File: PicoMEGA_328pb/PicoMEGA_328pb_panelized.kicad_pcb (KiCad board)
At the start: 2 copper layers, 100.2 x 94.2 mm, 416 parts, among them J1 ICSP, J2 3V3, J3 GPIO BLK A, J4 GPIO BLK B, J5 GPIO BLK C, J6 GPIO BLK D, U1 TPS62745DSSR, U2 ATmega328PB-MU, Y1 8Mhz

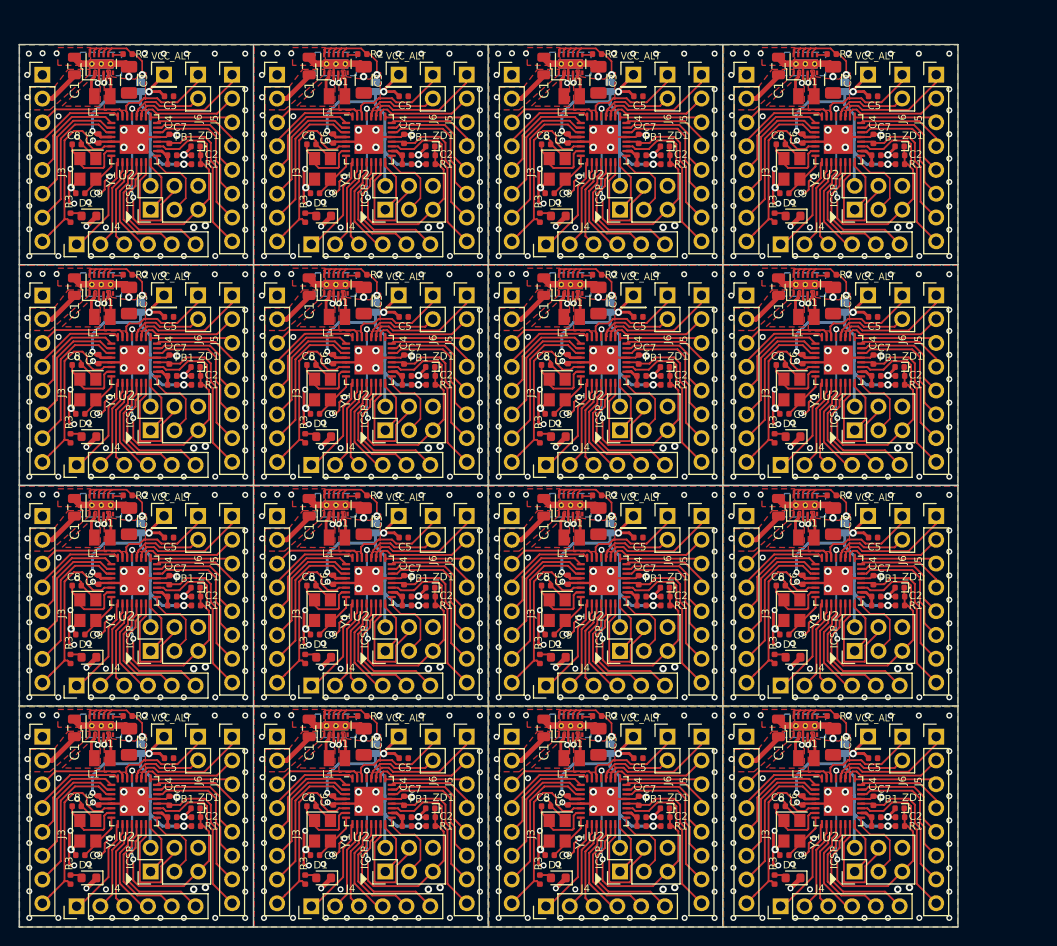
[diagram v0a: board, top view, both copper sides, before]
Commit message: PicoMEGA 328PB: rev0.1d
Fixed V_in regulator to use input voltage for enable to gurantee the
regulator powers on when an input voltage is applied.
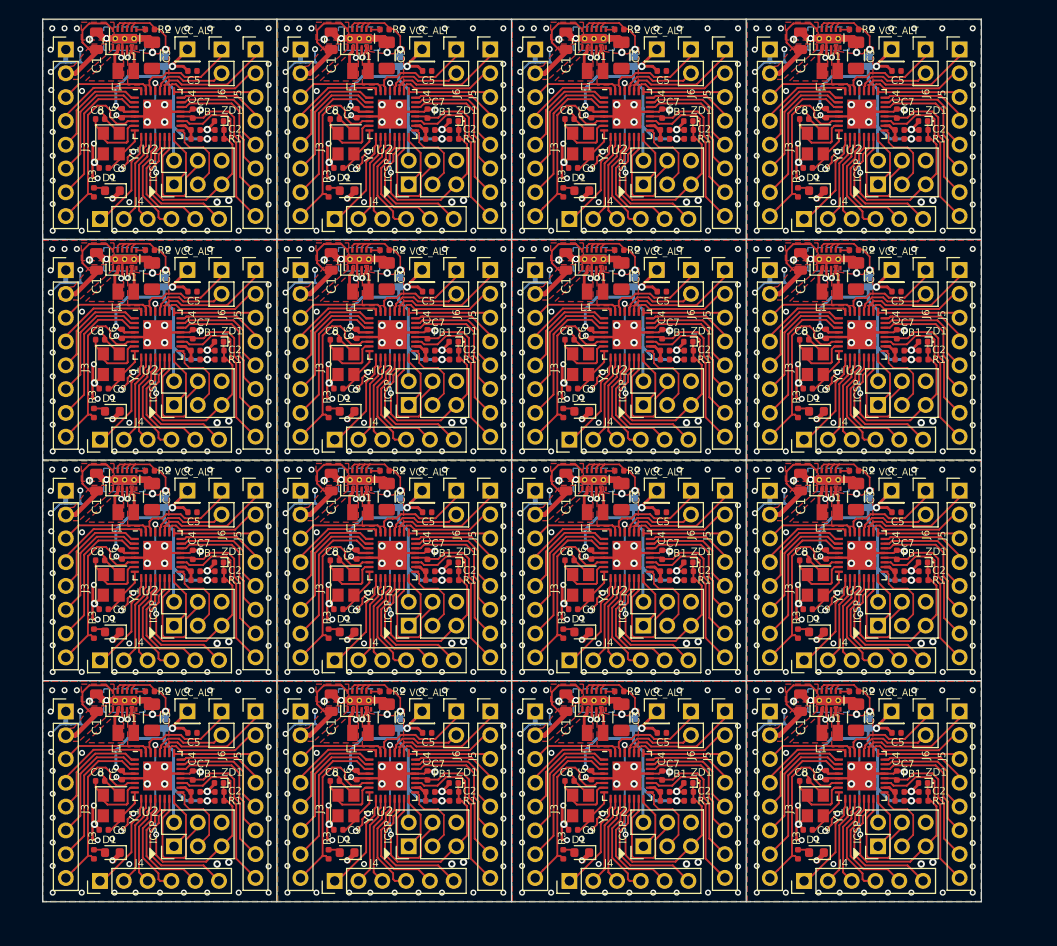
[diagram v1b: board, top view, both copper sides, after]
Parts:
- removed the C1 at (172.0, 124.6)
- removed the C1 at (121.9, 101.1)
- removed the C1 at (121.9, 77.5)
- removed the C1 at (121.9, 54.0)
- removed the C1 at (96.9, 124.6)
- removed the C1 at (96.9, 101.1)
- removed the C1 at (96.9, 77.5)
- removed the C1 at (172.0, 101.1)
- removed the C1 at (172.0, 77.5)
- removed the C1 at (172.0, 54.0)
- removed the C1 at (147.0, 124.6)
- removed the C1 at (147.0, 101.1)
- removed the C1 at (147.0, 77.5)
- removed the C1 at (147.0, 54.0)
- removed the C1 at (121.9, 124.6)
- removed the C2 at (185.0, 134.2)
- removed the C2 at (134.9, 110.6)
- removed the C2 at (134.9, 87.1)
- removed the C2 at (134.9, 63.5)
- removed the C2 at (109.8, 134.2)
- removed the C2 at (109.8, 110.6)
- removed the C2 at (109.8, 87.1)
- removed the C2 at (185.0, 110.6)
- removed the C2 at (185.0, 87.1)
- removed the C2 at (185.0, 63.5)
- removed the C2 at (160.0, 134.2)
- removed the C2 at (160.0, 110.6)
- removed the C2 at (160.0, 87.1)
- removed the C2 at (160.0, 63.5)
- removed the C2 at (134.9, 134.2)
- removed the C3 at (177.9, 126.1)
- removed the C3 at (127.8, 102.6)
- removed the C3 at (127.8, 79.0)
- removed the C3 at (127.8, 55.5)
- removed the C3 at (102.7, 126.1)
- removed the C3 at (102.7, 102.6)
- removed the C3 at (102.7, 79.0)
- removed the C3 at (177.9, 102.6)
- removed the C3 at (177.9, 79.0)
- removed the C3 at (177.9, 55.5)
- removed the C3 at (152.8, 126.1)
- removed the C3 at (152.8, 102.6)
- removed the C3 at (152.8, 79.0)
- removed the C3 at (152.8, 55.5)
- removed the C3 at (127.8, 126.1)
- removed the C4 at (182.2, 132.4)
- removed the C4 at (132.1, 108.9)
- removed the C4 at (132.1, 85.3)
- removed the C4 at (132.1, 61.8)
- removed the C4 at (107.0, 132.4)
- removed the C4 at (107.0, 108.9)
- removed the C4 at (107.0, 85.3)
- removed the C4 at (182.2, 108.9)
- removed the C4 at (182.2, 85.3)
- removed the C4 at (182.2, 61.8)
- removed the C4 at (157.1, 132.4)
- removed the C4 at (157.1, 108.9)
- removed the C4 at (157.1, 85.3)
- removed the C4 at (157.1, 61.8)
- removed the C4 at (132.1, 132.4)
- removed the C5 at (182.1, 127.9)
- removed the C5 at (132.0, 104.3)
- removed the C5 at (132.0, 80.8)
- removed the C5 at (132.0, 57.2)
- removed the C5 at (107.0, 127.9)
- removed the C5 at (107.0, 104.3)
- removed the C5 at (107.0, 80.8)
- removed the C5 at (182.1, 104.3)
- removed the C5 at (182.1, 80.8)
- removed the C5 at (182.1, 57.2)
- removed the C5 at (157.1, 127.9)
- removed the C5 at (157.1, 104.3)
- removed the C5 at (157.1, 80.8)
- removed the C5 at (157.1, 57.2)
- removed the C5 at (132.0, 127.9)
- removed the C6 at (174.6, 132.4)
- removed the C6 at (124.5, 108.8)
- removed the C6 at (124.5, 85.3)
- removed the C6 at (124.5, 61.7)
- removed the C6 at (99.5, 132.4)
- removed the C6 at (99.5, 108.8)
- removed the C6 at (99.5, 85.3)
- removed the C6 at (174.6, 108.8)
- removed the C6 at (174.6, 85.3)
- removed the C6 at (174.6, 61.7)
- removed the C6 at (149.6, 132.4)
- removed the C6 at (149.6, 108.8)
- removed the C6 at (149.6, 85.3)
- removed the C6 at (149.6, 61.7)
- removed the C6 at (124.5, 132.4)
- removed the C7 at (182.5, 134.2)
- removed the C7 at (132.4, 110.6)
- removed the C7 at (132.4, 87.1)
- removed the C7 at (132.4, 63.5)
- removed the C7 at (107.3, 134.2)
- removed the C7 at (107.3, 110.6)
- removed the C7 at (107.3, 87.1)
- removed the C7 at (182.5, 110.6)
- removed the C7 at (182.5, 87.1)
- removed the C7 at (182.5, 63.5)
- removed the C7 at (157.4, 134.2)
- removed the C7 at (157.4, 110.6)
- removed the C7 at (157.4, 87.1)
- removed the C7 at (157.4, 63.5)
- removed the C7 at (132.4, 134.2)
- removed the C8 at (172.3, 133.0)
- removed the C8 at (122.2, 109.4)
- removed the C8 at (122.2, 85.9)
- removed the C8 at (122.2, 62.3)
- removed the C8 at (97.1, 133.0)
- removed the C8 at (97.1, 109.4)
- removed the C8 at (97.1, 85.9)
- removed the C8 at (172.3, 109.4)
- removed the C8 at (172.3, 85.9)
- removed the C8 at (172.3, 62.3)
- removed the C8 at (147.2, 133.0)
- removed the C8 at (147.2, 109.4)
- removed the C8 at (147.2, 85.9)
- removed the C8 at (147.2, 62.3)
- removed the C8 at (122.2, 133.0)
- removed the C9 at (172.7, 138.2)
- removed the C9 at (122.6, 114.7)
- removed the C9 at (122.6, 91.1)
- removed the C9 at (122.6, 67.5)
- removed the C9 at (97.5, 138.2)
- removed the C9 at (97.5, 114.7)
- removed the C9 at (97.5, 91.1)
- removed the C9 at (172.7, 114.7)
- removed the C9 at (172.7, 91.1)
- removed the C9 at (172.7, 67.5)
- removed the C9 at (147.6, 138.2)
- removed the C9 at (147.6, 114.7)
- removed the C9 at (147.6, 91.1)
- removed the C9 at (147.6, 67.5)
- removed the C9 at (122.6, 138.2)
- removed the D1 at (173.6, 140.6)
- removed the D1 at (123.5, 117.1)
- removed the D1 at (123.5, 93.5)
- removed the D1 at (123.5, 70.0)
- removed the D1 at (98.4, 140.6)
- removed the D1 at (98.4, 117.1)
- removed the D1 at (98.4, 93.5)
- removed the D1 at (173.6, 117.1)
- removed the D1 at (173.6, 93.5)
- removed the D1 at (173.6, 70.0)
- removed the D1 at (148.5, 140.6)
- removed the D1 at (148.5, 117.1)
- removed the D1 at (148.5, 93.5)
- removed the D1 at (148.5, 70.0)
- removed the D1 at (123.5, 140.6)
- removed the FB1 at (182.5, 135.1)
- removed the FB1 at (132.4, 111.6)
- removed the FB1 at (132.4, 88.0)
- removed the FB1 at (132.4, 64.5)
- removed the FB1 at (107.3, 135.1)
- removed the FB1 at (107.3, 111.6)
- removed the FB1 at (107.3, 88.0)
- removed the FB1 at (182.5, 111.6)
- removed the FB1 at (182.5, 88.0)
- removed the FB1 at (182.5, 64.5)
- removed the FB1 at (157.4, 135.1)
- removed the FB1 at (157.4, 111.6)
- removed the FB1 at (157.4, 88.0)
- removed the FB1 at (157.4, 64.5)
- removed the FB1 at (132.4, 135.1)
- removed the J1 at (180.2, 140.0)
- removed the J1 at (130.1, 116.4)
- removed the J1 at (130.1, 92.9)
- removed the J1 at (130.1, 69.3)
- removed the J1 at (105.0, 140.0)
- removed the J1 at (105.0, 116.4)
- removed the J1 at (105.0, 92.9)
- removed the J1 at (180.2, 116.4)
- removed the J1 at (180.2, 92.9)
- removed the J1 at (180.2, 69.3)
- removed the J1 at (155.1, 140.0)
- removed the J1 at (155.1, 116.4)
- removed the J1 at (155.1, 92.9)
- removed the J1 at (155.1, 69.3)
- removed the J1 at (130.1, 140.0)
- removed the J2 at (181.6, 125.5)
- removed the J2 at (131.5, 102.0)
- removed the J2 at (131.5, 78.4)
- removed the J2 at (131.5, 54.9)
- removed the J2 at (106.4, 125.5)
- removed the J2 at (106.4, 102.0)
- removed the J2 at (106.4, 78.4)
- removed the J2 at (181.6, 102.0)
- removed the J2 at (181.6, 78.4)
- removed the J2 at (181.6, 54.9)
- removed the J2 at (156.5, 125.5)
- removed the J2 at (156.5, 102.0)
- removed the J2 at (156.5, 78.4)
- removed the J2 at (156.5, 54.9)
- removed the J2 at (131.5, 125.5)
- removed the J3 at (168.6, 125.6)
- removed the J3 at (118.5, 102.0)
- removed the J3 at (118.5, 78.5)
- removed the J3 at (118.5, 54.9)
- removed the J3 at (93.5, 125.6)
- removed the J3 at (93.5, 102.0)
- removed the J3 at (93.5, 78.5)
- removed the J3 at (168.6, 102.0)
- removed the J3 at (168.6, 78.5)
- removed the J3 at (168.6, 54.9)
- removed the J3 at (143.6, 125.6)
- removed the J3 at (143.6, 102.0)
- removed the J3 at (143.6, 78.5)
- removed the J3 at (143.6, 54.9)
- removed the J3 at (118.5, 125.6)
- removed the J4 at (172.3, 143.7)
- removed the J4 at (122.2, 120.1)
- removed the J4 at (122.2, 96.6)
- removed the J4 at (122.2, 73.0)
- removed the J4 at (97.1, 143.7)
- removed the J4 at (97.1, 120.1)
- removed the J4 at (97.1, 96.6)
- removed the J4 at (172.3, 120.1)
- removed the J4 at (172.3, 96.6)
- removed the J4 at (172.3, 73.0)
- removed the J4 at (147.2, 143.7)
- removed the J4 at (147.2, 120.1)
- removed the J4 at (147.2, 96.6)
- removed the J4 at (147.2, 73.0)
- removed the J4 at (122.2, 143.7)
- removed the J5 at (188.9, 125.6)
- removed the J5 at (138.8, 102.0)
- removed the J5 at (138.8, 78.5)
- removed the J5 at (138.8, 54.9)
- removed the J5 at (113.7, 125.6)
- removed the J5 at (113.7, 102.0)
- removed the J5 at (113.7, 78.5)
- removed the J5 at (188.9, 102.0)
- removed the J5 at (188.9, 78.5)
- removed the J5 at (188.9, 54.9)
- removed the J5 at (163.8, 125.6)
- removed the J5 at (163.8, 102.0)
- removed the J5 at (163.8, 78.5)
- removed the J5 at (163.8, 54.9)
- removed the J5 at (138.8, 125.6)
- removed the J6 at (185.2, 125.6)
- removed the J6 at (135.1, 102.0)
- removed the J6 at (135.1, 78.5)
- removed the J6 at (135.1, 54.9)
- removed the J6 at (110.1, 125.6)
- removed the J6 at (110.1, 102.0)
- removed the J6 at (110.1, 78.5)
- removed the J6 at (185.2, 102.0)
- removed the J6 at (185.2, 78.5)
- removed the J6 at (185.2, 54.9)
- removed the J6 at (160.2, 125.6)
- removed the J6 at (160.2, 102.0)
- removed the J6 at (160.2, 78.5)
- removed the J6 at (160.2, 54.9)
- removed the J6 at (135.1, 125.6)
- removed the JP1 at (179.1, 126.9)
- removed the JP1 at (129.0, 103.3)
- removed the JP1 at (129.0, 79.8)
- removed the JP1 at (129.0, 56.2)
- removed the JP1 at (103.9, 126.9)
- removed the JP1 at (103.9, 103.3)
- removed the JP1 at (103.9, 79.8)
- removed the JP1 at (179.1, 103.3)
- removed the JP1 at (179.1, 79.8)
- removed the JP1 at (179.1, 56.2)
- removed the JP1 at (154.0, 126.9)
- removed the JP1 at (154.0, 103.3)
- removed the JP1 at (154.0, 79.8)
- removed the JP1 at (154.0, 56.2)
- removed the JP1 at (129.0, 126.9)
- removed the L1 at (175.0, 127.9)
- removed the L1 at (124.9, 104.3)
- removed the L1 at (124.9, 80.8)
- removed the L1 at (124.9, 57.2)
- removed the L1 at (99.8, 127.9)
- removed the L1 at (99.8, 104.3)
- removed the L1 at (99.8, 80.8)
- removed the L1 at (175.0, 104.3)
- removed the L1 at (175.0, 80.8)
- removed the L1 at (175.0, 57.2)
- removed the L1 at (149.9, 127.9)
- removed the L1 at (149.9, 104.3)
- removed the L1 at (149.9, 80.8)
- removed the L1 at (149.9, 57.2)
- removed the L1 at (124.9, 127.9)
- removed the R1 at (185.0, 135.1)
- removed the R1 at (134.9, 111.6)
- removed the R1 at (134.9, 88.0)
- removed the R1 at (134.9, 64.5)
- removed the R1 at (109.8, 135.1)
- removed the R1 at (109.8, 111.6)
- removed the R1 at (109.8, 88.0)
- removed the R1 at (185.0, 111.6)
- removed the R1 at (185.0, 88.0)
- removed the R1 at (185.0, 64.5)
- removed the R1 at (160.0, 135.1)
- removed the R1 at (160.0, 111.6)
- removed the R1 at (160.0, 88.0)
- removed the R1 at (160.0, 64.5)
- removed the R1 at (134.9, 135.1)
- removed the R2 at (177.7, 123.4)
- removed the R2 at (127.6, 99.8)
- removed the R2 at (127.6, 76.3)
- removed the R2 at (127.6, 52.7)
- removed the R2 at (102.5, 123.4)
- removed the R2 at (102.5, 99.8)
- removed the R2 at (102.5, 76.3)
- removed the R2 at (177.7, 99.8)
- removed the R2 at (177.7, 76.3)
- removed the R2 at (177.7, 52.7)
- removed the R2 at (152.7, 123.4)
- removed the R2 at (152.7, 99.8)
- removed the R2 at (152.7, 76.3)
- removed the R2 at (152.7, 52.7)
- removed the R2 at (127.6, 123.4)
- removed the R3 at (171.6, 140.8)
- removed the R3 at (121.5, 117.3)
- removed the R3 at (121.5, 93.7)
- removed the R3 at (121.5, 70.2)
- removed the R3 at (96.5, 140.8)
- removed the R3 at (96.5, 117.3)
- removed the R3 at (96.5, 93.7)
- removed the R3 at (171.6, 117.3)
- removed the R3 at (171.6, 93.7)
- removed the R3 at (171.6, 70.2)
- removed the R3 at (146.6, 140.8)
- removed the R3 at (146.6, 117.3)
- removed the R3 at (146.6, 93.7)
- removed the R3 at (146.6, 70.2)
- removed the R3 at (121.5, 140.8)
- removed the U1 at (174.9, 124.4)
- removed the U1 at (124.8, 100.8)
- removed the U1 at (124.8, 77.3)
- removed the U1 at (124.8, 53.7)
- removed the U1 at (99.7, 124.4)
- removed the U1 at (99.7, 100.8)
- removed the U1 at (99.7, 77.3)
- removed the U1 at (174.9, 100.8)
- removed the U1 at (174.9, 77.3)
- removed the U1 at (174.9, 53.7)
- removed the U1 at (149.8, 124.4)
- removed the U1 at (149.8, 100.8)
- removed the U1 at (149.8, 77.3)
- removed the U1 at (149.8, 53.7)
- removed the U1 at (124.8, 124.4)
- removed the U2 at (178.4, 132.5)
- removed the U2 at (128.3, 108.9)
- removed the U2 at (128.3, 85.4)
- removed the U2 at (128.3, 61.8)
- removed the U2 at (103.2, 132.5)
- removed the U2 at (103.2, 108.9)
- removed the U2 at (103.2, 85.4)
- removed the U2 at (178.4, 108.9)
- removed the U2 at (178.4, 85.4)
- removed the U2 at (178.4, 61.8)
- removed the U2 at (153.4, 132.5)
- removed the U2 at (153.4, 108.9)
- removed the U2 at (153.4, 85.4)
- removed the U2 at (153.4, 61.8)
- removed the U2 at (128.3, 132.5)
- removed the Y1 at (173.5, 135.6)
- removed the Y1 at (123.4, 112.1)
- removed the Y1 at (123.4, 88.5)
- removed the Y1 at (123.4, 65.0)
- removed the Y1 at (98.3, 135.6)
- removed the Y1 at (98.3, 112.1)
- removed the Y1 at (98.3, 88.5)
- removed the Y1 at (173.5, 112.1)
- removed the Y1 at (173.5, 88.5)
- removed the Y1 at (173.5, 65.0)
- removed the Y1 at (148.4, 135.6)
- removed the Y1 at (148.4, 112.1)
- removed the Y1 at (148.4, 88.5)
- removed the Y1 at (148.4, 65.0)
- removed the Y1 at (123.4, 135.6)
- removed the ZD1 at (185.0, 133.2)
- removed the ZD1 at (134.9, 109.7)
- removed the ZD1 at (134.9, 86.1)
- removed the ZD1 at (134.9, 62.5)
- removed the ZD1 at (109.8, 133.2)
- removed the ZD1 at (109.8, 109.7)
- removed the ZD1 at (109.8, 86.1)
- removed the ZD1 at (185.0, 109.7)
- removed the ZD1 at (185.0, 86.1)
- removed the ZD1 at (185.0, 62.5)
- removed the ZD1 at (159.9, 133.2)
- removed the ZD1 at (159.9, 109.7)
- removed the ZD1 at (159.9, 86.1)
- removed the ZD1 at (159.9, 62.5)
- removed the ZD1 at (134.9, 133.2)
- added C1: 10u, Capacitor_SMD:C_0805_2012Metric, F.Cu at (174.4, 121.9)
- added C1: 10u, Capacitor_SMD:C_0805_2012Metric, F.Cu at (124.3, 98.4)
- added C1: 10u, Capacitor_SMD:C_0805_2012Metric, F.Cu at (124.3, 74.8)
- added C1: 10u, Capacitor_SMD:C_0805_2012Metric, F.Cu at (124.3, 51.3)
- added C1: 10u, Capacitor_SMD:C_0805_2012Metric, F.Cu at (99.2, 121.9)
- added C1: 10u, Capacitor_SMD:C_0805_2012Metric, F.Cu at (99.2, 98.4)
- added C1: 10u, Capacitor_SMD:C_0805_2012Metric, F.Cu at (99.2, 74.8)
- added C1: 10u, Capacitor_SMD:C_0805_2012Metric, F.Cu at (174.4, 98.4)
- added C1: 10u, Capacitor_SMD:C_0805_2012Metric, F.Cu at (174.4, 74.8)
- added C1: 10u, Capacitor_SMD:C_0805_2012Metric, F.Cu at (174.4, 51.3)
- added C1: 10u, Capacitor_SMD:C_0805_2012Metric, F.Cu at (149.3, 121.9)
- added C1: 10u, Capacitor_SMD:C_0805_2012Metric, F.Cu at (149.3, 98.4)
- added C1: 10u, Capacitor_SMD:C_0805_2012Metric, F.Cu at (149.3, 74.8)
- added C1: 10u, Capacitor_SMD:C_0805_2012Metric, F.Cu at (149.3, 51.3)
- added C1: 10u, Capacitor_SMD:C_0805_2012Metric, F.Cu at (124.3, 121.9)
- added C2: 0.1u, Capacitor_SMD:C_0402_1005Metric, F.Cu at (187.5, 131.5)
- added C2: 0.1u, Capacitor_SMD:C_0402_1005Metric, F.Cu at (137.4, 107.9)
- added C2: 0.1u, Capacitor_SMD:C_0402_1005Metric, F.Cu at (137.4, 84.4)
- added C2: 0.1u, Capacitor_SMD:C_0402_1005Metric, F.Cu at (137.4, 60.8)
- added C2: 0.1u, Capacitor_SMD:C_0402_1005Metric, F.Cu at (112.3, 131.5)
- added C2: 0.1u, Capacitor_SMD:C_0402_1005Metric, F.Cu at (112.3, 107.9)
- added C2: 0.1u, Capacitor_SMD:C_0402_1005Metric, F.Cu at (112.3, 84.4)
- added C2: 0.1u, Capacitor_SMD:C_0402_1005Metric, F.Cu at (187.5, 107.9)
- added C2: 0.1u, Capacitor_SMD:C_0402_1005Metric, F.Cu at (187.5, 84.4)
- added C2: 0.1u, Capacitor_SMD:C_0402_1005Metric, F.Cu at (187.5, 60.8)
- added C2: 0.1u, Capacitor_SMD:C_0402_1005Metric, F.Cu at (162.5, 131.5)
- added C2: 0.1u, Capacitor_SMD:C_0402_1005Metric, F.Cu at (162.5, 107.9)
- added C2: 0.1u, Capacitor_SMD:C_0402_1005Metric, F.Cu at (162.5, 84.4)
- added C2: 0.1u, Capacitor_SMD:C_0402_1005Metric, F.Cu at (162.5, 60.8)
- added C2: 0.1u, Capacitor_SMD:C_0402_1005Metric, F.Cu at (137.4, 131.5)
- added C3: 22u, Capacitor_SMD:C_1206_3216Metric, F.Cu at (180.3, 123.5)
- added C3: 22u, Capacitor_SMD:C_1206_3216Metric, F.Cu at (130.2, 99.9)
- added C3: 22u, Capacitor_SMD:C_1206_3216Metric, F.Cu at (130.2, 76.4)
- added C3: 22u, Capacitor_SMD:C_1206_3216Metric, F.Cu at (130.2, 52.8)
- added C3: 22u, Capacitor_SMD:C_1206_3216Metric, F.Cu at (105.2, 123.5)
- added C3: 22u, Capacitor_SMD:C_1206_3216Metric, F.Cu at (105.2, 99.9)
- added C3: 22u, Capacitor_SMD:C_1206_3216Metric, F.Cu at (105.2, 76.4)
- added C3: 22u, Capacitor_SMD:C_1206_3216Metric, F.Cu at (180.3, 99.9)
- added C3: 22u, Capacitor_SMD:C_1206_3216Metric, F.Cu at (180.3, 76.4)
- added C3: 22u, Capacitor_SMD:C_1206_3216Metric, F.Cu at (180.3, 52.8)
- added C3: 22u, Capacitor_SMD:C_1206_3216Metric, F.Cu at (155.3, 123.5)
- added C3: 22u, Capacitor_SMD:C_1206_3216Metric, F.Cu at (155.3, 99.9)
- added C3: 22u, Capacitor_SMD:C_1206_3216Metric, F.Cu at (155.3, 76.4)
- added C3: 22u, Capacitor_SMD:C_1206_3216Metric, F.Cu at (155.3, 52.8)
- added C3: 22u, Capacitor_SMD:C_1206_3216Metric, F.Cu at (130.2, 123.5)
- added C4: 0.1u, Capacitor_SMD:C_0402_1005Metric, F.Cu at (184.7, 129.7)
- added C4: 0.1u, Capacitor_SMD:C_0402_1005Metric, F.Cu at (134.6, 106.2)
- added C4: 0.1u, Capacitor_SMD:C_0402_1005Metric, F.Cu at (134.6, 82.6)
- added C4: 0.1u, Capacitor_SMD:C_0402_1005Metric, F.Cu at (134.6, 59.0)
- added C4: 0.1u, Capacitor_SMD:C_0402_1005Metric, F.Cu at (109.5, 129.7)
- added C4: 0.1u, Capacitor_SMD:C_0402_1005Metric, F.Cu at (109.5, 106.2)
- added C4: 0.1u, Capacitor_SMD:C_0402_1005Metric, F.Cu at (109.5, 82.6)
- added C4: 0.1u, Capacitor_SMD:C_0402_1005Metric, F.Cu at (184.7, 106.2)
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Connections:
- U1 pad 12: /3V3_REG -> +9V
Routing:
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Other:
- board text added: "PicoMEGA 328PB Rev 0.1d Jun 2020"
- board text removed: "PicoMEGA 328PB Rev 0.1c Jun 2020"

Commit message: PicoMEGA 328PB: rev0.1e
Revised clock area to use guard ring to prevent cross-talk interference
for adjacent GPIO traces. No such protection of the GPIOs themselves
though.
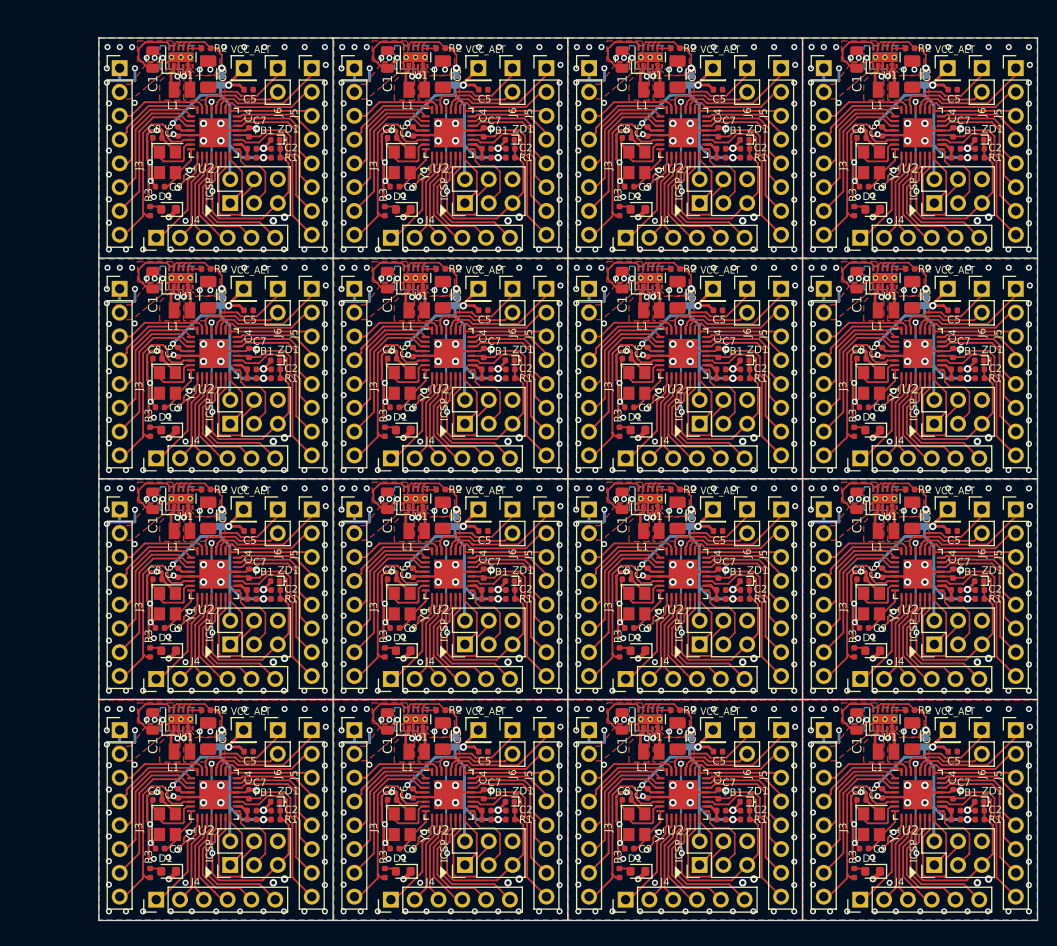
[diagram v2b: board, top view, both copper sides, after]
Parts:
- removed the C1 at (174.4, 121.9)
- removed the C1 at (124.3, 98.4)
- removed the C1 at (124.3, 74.8)
- removed the C1 at (124.3, 51.3)
- removed the C1 at (99.2, 121.9)
- removed the C1 at (99.2, 98.4)
- removed the C1 at (99.2, 74.8)
- removed the C1 at (174.4, 98.4)
- removed the C1 at (174.4, 74.8)
- removed the C1 at (174.4, 51.3)
- removed the C1 at (149.3, 121.9)
- removed the C1 at (149.3, 98.4)
- removed the C1 at (149.3, 74.8)
- removed the C1 at (149.3, 51.3)
- removed the C1 at (124.3, 121.9)
- removed the C2 at (187.5, 131.5)
- removed the C2 at (137.4, 107.9)
- removed the C2 at (137.4, 84.4)
- removed the C2 at (137.4, 60.8)
- removed the C2 at (112.3, 131.5)
- removed the C2 at (112.3, 107.9)
- removed the C2 at (112.3, 84.4)
- removed the C2 at (187.5, 107.9)
- removed the C2 at (187.5, 84.4)
- removed the C2 at (187.5, 60.8)
- removed the C2 at (162.5, 131.5)
- removed the C2 at (162.5, 107.9)
- removed the C2 at (162.5, 84.4)
- removed the C2 at (162.5, 60.8)
- removed the C2 at (137.4, 131.5)
- removed the C3 at (180.3, 123.5)
- removed the C3 at (130.2, 99.9)
- removed the C3 at (130.2, 76.4)
- removed the C3 at (130.2, 52.8)
- removed the C3 at (105.2, 123.5)
- removed the C3 at (105.2, 99.9)
- removed the C3 at (105.2, 76.4)
- removed the C3 at (180.3, 99.9)
- removed the C3 at (180.3, 76.4)
- removed the C3 at (180.3, 52.8)
- removed the C3 at (155.3, 123.5)
- removed the C3 at (155.3, 99.9)
- removed the C3 at (155.3, 76.4)
- removed the C3 at (155.3, 52.8)
- removed the C3 at (130.2, 123.5)
- removed the C4 at (184.7, 129.7)
- removed the C4 at (134.6, 106.2)
- removed the C4 at (134.6, 82.6)
- removed the C4 at (134.6, 59.0)
- removed the C4 at (109.5, 129.7)
- removed the C4 at (109.5, 106.2)
- removed the C4 at (109.5, 82.6)
- removed the C4 at (184.7, 106.2)
- removed the C4 at (184.7, 82.6)
- removed the C4 at (184.7, 59.0)
- removed the C4 at (159.6, 129.7)
- removed the C4 at (159.6, 106.2)
- removed the C4 at (159.6, 82.6)
- removed the C4 at (159.6, 59.0)
- removed the C4 at (134.6, 129.7)
- removed the C5 at (184.6, 125.2)
- removed the C5 at (134.5, 101.6)
- removed the C5 at (134.5, 78.1)
- removed the C5 at (134.5, 54.5)
- removed the C5 at (109.5, 125.2)
- removed the C5 at (109.5, 101.6)
- removed the C5 at (109.5, 78.1)
- removed the C5 at (184.6, 101.6)
- removed the C5 at (184.6, 78.1)
- removed the C5 at (184.6, 54.5)
- removed the C5 at (159.6, 125.2)
- removed the C5 at (159.6, 101.6)
- removed the C5 at (159.6, 78.1)
- removed the C5 at (159.6, 54.5)
- removed the C5 at (134.5, 125.2)
- removed the C6 at (177.1, 129.7)
- removed the C6 at (127.0, 106.1)
- removed the C6 at (127.0, 82.6)
- removed the C6 at (127.0, 59.0)
- removed the C6 at (102.0, 129.7)
- removed the C6 at (102.0, 106.1)
- removed the C6 at (102.0, 82.6)
- removed the C6 at (177.1, 106.1)
- removed the C6 at (177.1, 82.6)
- removed the C6 at (177.1, 59.0)
- removed the C6 at (152.1, 129.7)
- removed the C6 at (152.1, 106.1)
- removed the C6 at (152.1, 82.6)
- removed the C6 at (152.1, 59.0)
- removed the C6 at (127.0, 129.7)
- removed the C7 at (185.0, 131.5)
- removed the C7 at (134.9, 107.9)
- removed the C7 at (134.9, 84.4)
- removed the C7 at (134.9, 60.8)
- removed the C7 at (109.8, 131.5)
- removed the C7 at (109.8, 107.9)
- removed the C7 at (109.8, 84.4)
- removed the C7 at (185.0, 107.9)
- removed the C7 at (185.0, 84.4)
- removed the C7 at (185.0, 60.8)
- removed the C7 at (159.9, 131.5)
- removed the C7 at (159.9, 107.9)
- removed the C7 at (159.9, 84.4)
- removed the C7 at (159.9, 60.8)
- removed the C7 at (134.9, 131.5)
- removed the C8 at (174.8, 130.3)
- removed the C8 at (124.7, 106.7)
- removed the C8 at (124.7, 83.2)
- removed the C8 at (124.7, 59.6)
- removed the C8 at (99.6, 130.3)
- removed the C8 at (99.6, 106.7)
- removed the C8 at (99.6, 83.2)
- removed the C8 at (174.8, 106.7)
- removed the C8 at (174.8, 83.2)
- removed the C8 at (174.8, 59.6)
- removed the C8 at (149.7, 130.3)
- removed the C8 at (149.7, 106.7)
- removed the C8 at (149.7, 83.2)
- removed the C8 at (149.7, 59.6)
- removed the C8 at (124.7, 130.3)
- removed the C9 at (175.2, 135.5)
- removed the C9 at (125.1, 112.0)
- removed the C9 at (125.1, 88.4)
- removed the C9 at (125.1, 64.8)
- removed the C9 at (100.0, 135.5)
- removed the C9 at (100.0, 112.0)
- removed the C9 at (100.0, 88.4)
- removed the C9 at (175.2, 112.0)
- removed the C9 at (175.2, 88.4)
- removed the C9 at (175.2, 64.8)
- removed the C9 at (150.1, 135.5)
- removed the C9 at (150.1, 112.0)
- removed the C9 at (150.1, 88.4)
- removed the C9 at (150.1, 64.8)
- removed the C9 at (125.1, 135.5)
- removed the D1 at (176.1, 137.9)
- removed the D1 at (126.0, 114.4)
- removed the D1 at (126.0, 90.8)
- removed the D1 at (126.0, 67.3)
- removed the D1 at (100.9, 137.9)
- removed the D1 at (100.9, 114.4)
- removed the D1 at (100.9, 90.8)
- removed the D1 at (176.1, 114.4)
- removed the D1 at (176.1, 90.8)
- removed the D1 at (176.1, 67.3)
- removed the D1 at (151.0, 137.9)
- removed the D1 at (151.0, 114.4)
- removed the D1 at (151.0, 90.8)
- removed the D1 at (151.0, 67.3)
- removed the D1 at (126.0, 137.9)
- removed the FB1 at (185.0, 132.4)
- removed the FB1 at (134.9, 108.9)
- removed the FB1 at (134.9, 85.3)
- removed the FB1 at (134.9, 61.8)
- removed the FB1 at (109.8, 132.4)
- removed the FB1 at (109.8, 108.9)
- removed the FB1 at (109.8, 85.3)
- removed the FB1 at (185.0, 108.9)
- removed the FB1 at (185.0, 85.3)
- removed the FB1 at (185.0, 61.8)
- removed the FB1 at (159.9, 132.4)
- removed the FB1 at (159.9, 108.9)
- removed the FB1 at (159.9, 85.3)
- removed the FB1 at (159.9, 61.8)
- removed the FB1 at (134.9, 132.4)
- removed the J1 at (182.7, 137.3)
- removed the J1 at (132.6, 113.7)
- removed the J1 at (132.6, 90.2)
- removed the J1 at (132.6, 66.6)
- removed the J1 at (107.5, 137.3)
- removed the J1 at (107.5, 113.7)
- removed the J1 at (107.5, 90.2)
- removed the J1 at (182.7, 113.7)
- removed the J1 at (182.7, 90.2)
- removed the J1 at (182.7, 66.6)
- removed the J1 at (157.6, 137.3)
- removed the J1 at (157.6, 113.7)
- removed the J1 at (157.6, 90.2)
- removed the J1 at (157.6, 66.6)
- removed the J1 at (132.6, 137.3)
- removed the J2 at (184.1, 122.8)
- removed the J2 at (134.0, 99.3)
- removed the J2 at (134.0, 75.7)
- removed the J2 at (134.0, 52.2)
- removed the J2 at (108.9, 122.8)
- removed the J2 at (108.9, 99.3)
- removed the J2 at (108.9, 75.7)
- removed the J2 at (184.1, 99.3)
- removed the J2 at (184.1, 75.7)
- removed the J2 at (184.1, 52.2)
- removed the J2 at (159.0, 122.8)
- removed the J2 at (159.0, 99.3)
- removed the J2 at (159.0, 75.7)
- removed the J2 at (159.0, 52.2)
- removed the J2 at (134.0, 122.8)
- removed the J3 at (171.1, 122.9)
- removed the J3 at (121.0, 99.3)
- removed the J3 at (121.0, 75.8)
- removed the J3 at (121.0, 52.2)
- removed the J3 at (96.0, 122.9)
- removed the J3 at (96.0, 99.3)
- removed the J3 at (96.0, 75.8)
- removed the J3 at (171.1, 99.3)
- removed the J3 at (171.1, 75.8)
- removed the J3 at (171.1, 52.2)
- removed the J3 at (146.1, 122.9)
- removed the J3 at (146.1, 99.3)
- removed the J3 at (146.1, 75.8)
- removed the J3 at (146.1, 52.2)
- removed the J3 at (121.0, 122.9)
- removed the J4 at (174.8, 141.0)
- removed the J4 at (124.7, 117.4)
- removed the J4 at (124.7, 93.9)
- removed the J4 at (124.7, 70.3)
- removed the J4 at (99.6, 141.0)
- removed the J4 at (99.6, 117.4)
- removed the J4 at (99.6, 93.9)
- removed the J4 at (174.8, 117.4)
- removed the J4 at (174.8, 93.9)
- removed the J4 at (174.8, 70.3)
- removed the J4 at (149.7, 141.0)
- removed the J4 at (149.7, 117.4)
- removed the J4 at (149.7, 93.9)
- removed the J4 at (149.7, 70.3)
- removed the J4 at (124.7, 141.0)
- removed the J5 at (191.4, 122.9)
- removed the J5 at (141.3, 99.3)
- removed the J5 at (141.3, 75.8)
- removed the J5 at (141.3, 52.2)
- removed the J5 at (116.2, 122.9)
- removed the J5 at (116.2, 99.3)
- removed the J5 at (116.2, 75.8)
- removed the J5 at (191.4, 99.3)
- removed the J5 at (191.4, 75.8)
- removed the J5 at (191.4, 52.2)
- removed the J5 at (166.3, 122.9)
- removed the J5 at (166.3, 99.3)
- removed the J5 at (166.3, 75.8)
- removed the J5 at (166.3, 52.2)
- removed the J5 at (141.3, 122.9)
- removed the J6 at (187.7, 122.9)
- removed the J6 at (137.6, 99.3)
- removed the J6 at (137.6, 75.8)
- removed the J6 at (137.6, 52.2)
- removed the J6 at (112.6, 122.9)
- removed the J6 at (112.6, 99.3)
- removed the J6 at (112.6, 75.8)
- removed the J6 at (187.7, 99.3)
- removed the J6 at (187.7, 75.8)
- removed the J6 at (187.7, 52.2)
- removed the J6 at (162.7, 122.9)
- removed the J6 at (162.7, 99.3)
- removed the J6 at (162.7, 75.8)
- removed the J6 at (162.7, 52.2)
- removed the J6 at (137.6, 122.9)
- removed the JP1 at (181.6, 124.2)
- removed the JP1 at (131.5, 100.6)
- removed the JP1 at (131.5, 77.1)
- removed the JP1 at (131.5, 53.5)
- removed the JP1 at (106.4, 124.2)
- removed the JP1 at (106.4, 100.6)
- removed the JP1 at (106.4, 77.1)
- removed the JP1 at (181.6, 100.6)
- removed the JP1 at (181.6, 77.1)
- removed the JP1 at (181.6, 53.5)
- removed the JP1 at (156.5, 124.2)
- removed the JP1 at (156.5, 100.6)
- removed the JP1 at (156.5, 77.1)
- removed the JP1 at (156.5, 53.5)
- removed the JP1 at (131.5, 124.2)
- removed the L1 at (177.5, 125.2)
- removed the L1 at (127.4, 101.6)
- removed the L1 at (127.4, 78.1)
- removed the L1 at (127.4, 54.5)
- removed the L1 at (102.3, 125.2)
- removed the L1 at (102.3, 101.6)
- removed the L1 at (102.3, 78.1)
- removed the L1 at (177.5, 101.6)
- removed the L1 at (177.5, 78.1)
- removed the L1 at (177.5, 54.5)
- removed the L1 at (152.4, 125.2)
- removed the L1 at (152.4, 101.6)
- removed the L1 at (152.4, 78.1)
- removed the L1 at (152.4, 54.5)
- removed the L1 at (127.4, 125.2)
- removed the R1 at (187.5, 132.4)
- removed the R1 at (137.4, 108.9)
- removed the R1 at (137.4, 85.3)
- removed the R1 at (137.4, 61.8)
- removed the R1 at (112.3, 132.4)
- removed the R1 at (112.3, 108.9)
- removed the R1 at (112.3, 85.3)
- removed the R1 at (187.5, 108.9)
- removed the R1 at (187.5, 85.3)
- removed the R1 at (187.5, 61.8)
- removed the R1 at (162.5, 132.4)
- removed the R1 at (162.5, 108.9)
- removed the R1 at (162.5, 85.3)
- removed the R1 at (162.5, 61.8)
- removed the R1 at (137.4, 132.4)
- removed the R2 at (180.1, 120.7)
- removed the R2 at (130.0, 97.2)
- removed the R2 at (130.0, 73.6)
- removed the R2 at (130.0, 50.1)
- removed the R2 at (104.9, 120.7)
- removed the R2 at (104.9, 97.2)
- removed the R2 at (104.9, 73.6)
- removed the R2 at (180.1, 97.2)
- removed the R2 at (180.1, 73.6)
- removed the R2 at (180.1, 50.1)
- removed the R2 at (155.0, 120.7)
- removed the R2 at (155.0, 97.2)
- removed the R2 at (155.0, 73.6)
- removed the R2 at (155.0, 50.1)
- removed the R2 at (130.0, 120.7)
- removed the R3 at (174.1, 138.1)
- removed the R3 at (124.0, 114.6)
- removed the R3 at (124.0, 91.0)
- removed the R3 at (124.0, 67.5)
- removed the R3 at (99.0, 138.1)
- removed the R3 at (99.0, 114.6)
- removed the R3 at (99.0, 91.0)
- removed the R3 at (174.1, 114.6)
- removed the R3 at (174.1, 91.0)
- removed the R3 at (174.1, 67.5)
- removed the R3 at (149.1, 138.1)
- removed the R3 at (149.1, 114.6)
- removed the R3 at (149.1, 91.0)
- removed the R3 at (149.1, 67.5)
- removed the R3 at (124.0, 138.1)
- removed the U1 at (177.4, 121.7)
- removed the U1 at (127.3, 98.1)
- removed the U1 at (127.3, 74.6)
- removed the U1 at (127.3, 51.0)
- removed the U1 at (102.2, 121.7)
- removed the U1 at (102.2, 98.1)
- removed the U1 at (102.2, 74.6)
- removed the U1 at (177.4, 98.1)
- removed the U1 at (177.4, 74.6)
- removed the U1 at (177.4, 51.0)
- removed the U1 at (152.3, 121.7)
- removed the U1 at (152.3, 98.1)
- removed the U1 at (152.3, 74.6)
- removed the U1 at (152.3, 51.0)
- removed the U1 at (127.3, 121.7)
- removed the U2 at (180.9, 129.8)
- removed the U2 at (130.8, 106.2)
- removed the U2 at (130.8, 82.7)
- removed the U2 at (130.8, 59.1)
- removed the U2 at (105.8, 129.8)
- removed the U2 at (105.8, 106.2)
- removed the U2 at (105.8, 82.7)
- removed the U2 at (180.9, 106.2)
- removed the U2 at (180.9, 82.7)
- removed the U2 at (180.9, 59.1)
- removed the U2 at (155.9, 129.8)
- removed the U2 at (155.9, 106.2)
- removed the U2 at (155.9, 82.7)
- removed the U2 at (155.9, 59.1)
- removed the U2 at (130.8, 129.8)
- removed the Y1 at (176.0, 132.9)
- removed the Y1 at (125.9, 109.4)
- removed the Y1 at (125.9, 85.8)
- removed the Y1 at (125.9, 62.2)
- removed the Y1 at (100.8, 132.9)
- removed the Y1 at (100.8, 109.4)
- removed the Y1 at (100.8, 85.8)
- removed the Y1 at (176.0, 109.4)
- removed the Y1 at (176.0, 85.8)
- removed the Y1 at (176.0, 62.2)
- removed the Y1 at (150.9, 132.9)
- removed the Y1 at (150.9, 109.4)
- removed the Y1 at (150.9, 85.8)
- removed the Y1 at (150.9, 62.2)
- removed the Y1 at (125.9, 132.9)
- removed the ZD1 at (187.5, 130.5)
- removed the ZD1 at (137.4, 107.0)
- removed the ZD1 at (137.4, 83.4)
- removed the ZD1 at (137.4, 59.9)
- removed the ZD1 at (112.3, 130.5)
- removed the ZD1 at (112.3, 107.0)
- removed the ZD1 at (112.3, 83.4)
- removed the ZD1 at (187.5, 107.0)
- removed the ZD1 at (187.5, 83.4)
- removed the ZD1 at (187.5, 59.9)
- removed the ZD1 at (162.4, 130.5)
- removed the ZD1 at (162.4, 107.0)
- removed the ZD1 at (162.4, 83.4)
- removed the ZD1 at (162.4, 59.9)
- removed the ZD1 at (137.4, 130.5)
- added C1: 10u, Capacitor_SMD:C_0805_2012Metric, F.Cu at (180.4, 123.9)
- added C1: 10u, Capacitor_SMD:C_0805_2012Metric, F.Cu at (130.3, 100.4)
- added C1: 10u, Capacitor_SMD:C_0805_2012Metric, F.Cu at (130.3, 76.8)
- added C1: 10u, Capacitor_SMD:C_0805_2012Metric, F.Cu at (130.3, 53.3)
- added C1: 10u, Capacitor_SMD:C_0805_2012Metric, F.Cu at (105.2, 123.9)
- added C1: 10u, Capacitor_SMD:C_0805_2012Metric, F.Cu at (105.2, 100.4)
- added C1: 10u, Capacitor_SMD:C_0805_2012Metric, F.Cu at (105.2, 76.8)
- added C1: 10u, Capacitor_SMD:C_0805_2012Metric, F.Cu at (180.4, 100.4)
- added C1: 10u, Capacitor_SMD:C_0805_2012Metric, F.Cu at (180.4, 76.8)
- added C1: 10u, Capacitor_SMD:C_0805_2012Metric, F.Cu at (180.4, 53.3)
- added C1: 10u, Capacitor_SMD:C_0805_2012Metric, F.Cu at (155.3, 123.9)
- added C1: 10u, Capacitor_SMD:C_0805_2012Metric, F.Cu at (155.3, 100.4)
- added C1: 10u, Capacitor_SMD:C_0805_2012Metric, F.Cu at (155.3, 76.8)
- added C1: 10u, Capacitor_SMD:C_0805_2012Metric, F.Cu at (155.3, 53.3)
- added C1: 10u, Capacitor_SMD:C_0805_2012Metric, F.Cu at (130.3, 123.9)
- added C2: 0.1u, Capacitor_SMD:C_0402_1005Metric, F.Cu at (193.5, 133.5)
- added C2: 0.1u, Capacitor_SMD:C_0402_1005Metric, F.Cu at (143.4, 109.9)
- added C2: 0.1u, Capacitor_SMD:C_0402_1005Metric, F.Cu at (143.4, 86.4)
- added C2: 0.1u, Capacitor_SMD:C_0402_1005Metric, F.Cu at (143.4, 62.8)
- added C2: 0.1u, Capacitor_SMD:C_0402_1005Metric, F.Cu at (118.3, 133.5)
- added C2: 0.1u, Capacitor_SMD:C_0402_1005Metric, F.Cu at (118.3, 109.9)
- added C2: 0.1u, Capacitor_SMD:C_0402_1005Metric, F.Cu at (118.3, 86.4)
- added C2: 0.1u, Capacitor_SMD:C_0402_1005Metric, F.Cu at (193.5, 109.9)
- added C2: 0.1u, Capacitor_SMD:C_0402_1005Metric, F.Cu at (193.5, 86.4)
- added C2: 0.1u, Capacitor_SMD:C_0402_1005Metric, F.Cu at (193.5, 62.8)
- added C2: 0.1u, Capacitor_SMD:C_0402_1005Metric, F.Cu at (168.5, 133.5)
- added C2: 0.1u, Capacitor_SMD:C_0402_1005Metric, F.Cu at (168.5, 109.9)
- added C2: 0.1u, Capacitor_SMD:C_0402_1005Metric, F.Cu at (168.5, 86.4)
- added C2: 0.1u, Capacitor_SMD:C_0402_1005Metric, F.Cu at (168.5, 62.8)
- added C2: 0.1u, Capacitor_SMD:C_0402_1005Metric, F.Cu at (143.4, 133.5)
- added C3: 22u, Capacitor_SMD:C_1206_3216Metric, F.Cu at (186.3, 125.5)
- added C3: 22u, Capacitor_SMD:C_1206_3216Metric, F.Cu at (136.2, 101.9)
- added C3: 22u, Capacitor_SMD:C_1206_3216Metric, F.Cu at (136.2, 78.4)
- added C3: 22u, Capacitor_SMD:C_1206_3216Metric, F.Cu at (136.2, 54.8)
- added C3: 22u, Capacitor_SMD:C_1206_3216Metric, F.Cu at (111.2, 125.5)
- added C3: 22u, Capacitor_SMD:C_1206_3216Metric, F.Cu at (111.2, 101.9)
- added C3: 22u, Capacitor_SMD:C_1206_3216Metric, F.Cu at (111.2, 78.4)
- added C3: 22u, Capacitor_SMD:C_1206_3216Metric, F.Cu at (186.3, 101.9)
- added C3: 22u, Capacitor_SMD:C_1206_3216Metric, F.Cu at (186.3, 78.4)
- added C3: 22u, Capacitor_SMD:C_1206_3216Metric, F.Cu at (186.3, 54.8)
- added C3: 22u, Capacitor_SMD:C_1206_3216Metric, F.Cu at (161.3, 125.5)
- added C3: 22u, Capacitor_SMD:C_1206_3216Metric, F.Cu at (161.3, 101.9)
- added C3: 22u, Capacitor_SMD:C_1206_3216Metric, F.Cu at (161.3, 78.4)
- added C3: 22u, Capacitor_SMD:C_1206_3216Metric, F.Cu at (161.3, 54.8)
- added C3: 22u, Capacitor_SMD:C_1206_3216Metric, F.Cu at (136.2, 125.5)
- added C4: 0.1u, Capacitor_SMD:C_0402_1005Metric, F.Cu at (190.7, 131.7)
- added C4: 0.1u, Capacitor_SMD:C_0402_1005Metric, F.Cu at (140.6, 108.2)
- added C4: 0.1u, Capacitor_SMD:C_0402_1005Metric, F.Cu at (140.6, 84.6)
- added C4: 0.1u, Capacitor_SMD:C_0402_1005Metric, F.Cu at (140.6, 61.0)
- added C4: 0.1u, Capacitor_SMD:C_0402_1005Metric, F.Cu at (115.5, 131.7)
- added C4: 0.1u, Capacitor_SMD:C_0402_1005Metric, F.Cu at (115.5, 108.2)
- added C4: 0.1u, Capacitor_SMD:C_0402_1005Metric, F.Cu at (115.5, 84.6)
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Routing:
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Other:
- board text added: ".\PicoMEGA_328pb_panelized.kicad_pcb (4x4 panel) generated with: ./panelizer.py --panelx=101 --panely=100 .\PicoMEGA_328pb.kicad_pcb"
- board text added: "PicoMEGA 328PB Rev 0.1e Jun 2020"
- board text removed: "PicoMEGA 328PB Rev 0.1d Jun 2020"
